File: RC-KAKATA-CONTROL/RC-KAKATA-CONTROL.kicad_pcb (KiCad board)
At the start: 4 copper layers, 160 x 160 mm, 178 parts, among them J1 Conn_02x20_Socket_DG250T-5.0-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, J10 DB125-2.54-4P-GN, J11 Screw_Terminal_01x02, J12 Conn_01x07, J13 Screw_Terminal_01x02, J15 Conn_01x12_Socket, J17 Screw_Terminal_01x02, J19 Screw_Terminal_01x02, J2 Screw_Terminal_01x02, J21 Screw_Terminal_01x02, J23 Screw_Terminal_01x02, J25 Conn_02x20_Socket_DG250T-5.0-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, J3 Screw_Terminal_01x02, J4 Screw_Terminal_01x02, J5 Screw_Terminal_01x02, J6 Raspberry_Pi_2x20_PTH, J7 Screw_Terminal_01x02, J8 DB125-2.54-4P-GN, J9 Screw_Terminal_01x02, SW1 TS-1088-AR02016, SW2 TS-1088-AR02016, SW3 TS-1088-AR02016, SW4 TS-1088-AR02016, SW6 TS-1088-AR02016, U1 PS-TO220, U13 ICM-20689, U2 PS-TO220, U3 STM32H743IIT6, U4 YK16S-L7.2-B10KA(32-8)-G-A29, U5 DB125-2.54-6P-GN, U8 W25Q128JVSIQTR, X1 SMD3225-4, X2 Q13MC3061000300

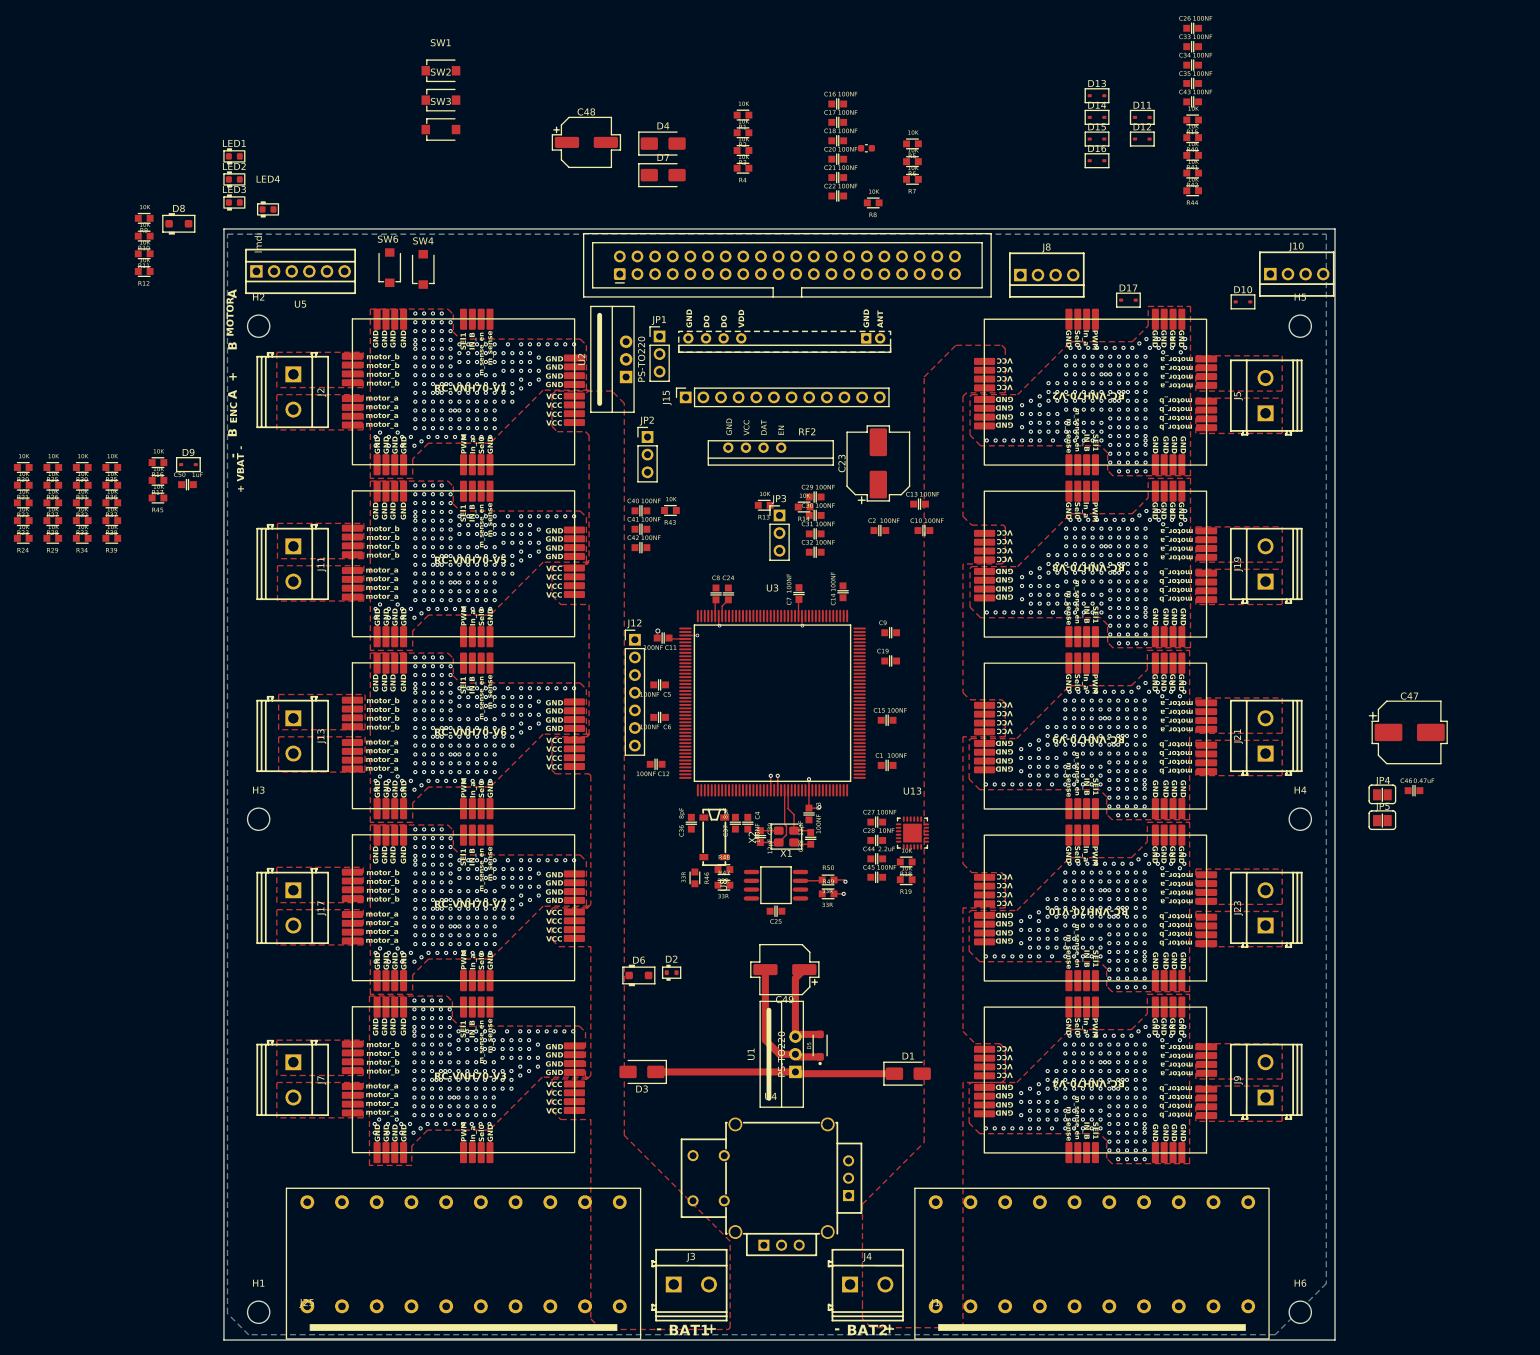
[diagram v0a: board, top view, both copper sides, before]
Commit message: Agregadas conexiones de analogicos Agregadas las conexiones de i2c Agregadas las conexiones de Uart Cambiados algunos detalles de tvs resistencias y cap Recolocados los componenetes de power supply Cambiados los diodos de entrada de la bateria por unos de 5A Cambios menores y mejorada la documentacion Agregada informacion en la serigrafia del PCB
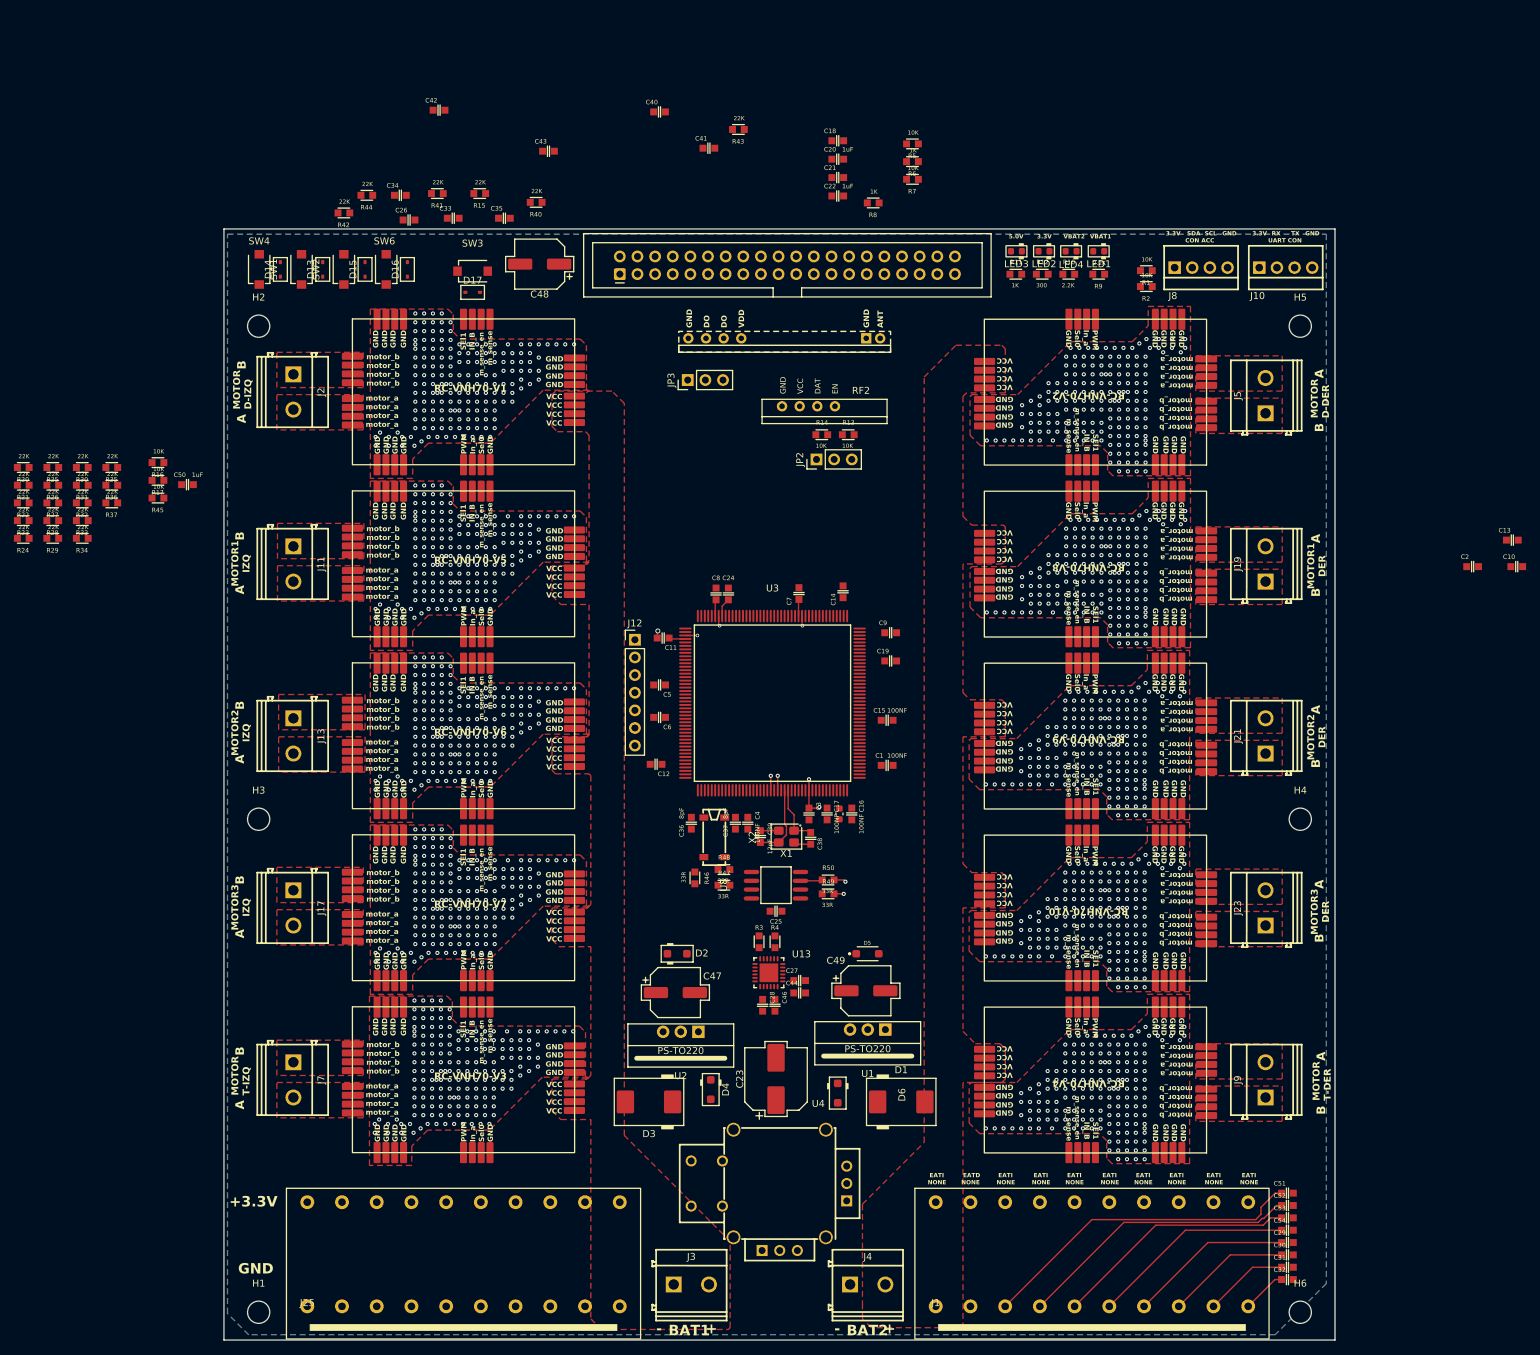
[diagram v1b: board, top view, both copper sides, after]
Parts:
- removed C45: 100NF, 4ms_Capacitor:C_0603
- removed D10, D11, D12, D9: PESD3V3L1BA, Diode_SMD_AKL:D_SOD-323_TVS
- removed D7: SS26, Diode_SMD:D_SMA
- removed D8: SMF24CA, Diode_SMD_AKL:D_SOD-123F
- removed J15: Conn_01x12_Socket, Connector_PinSocket_2.54mm:PinSocket_1x12_P2.54mm_Vertical
- removed JP1: Jumper_3_Bridged12, Connector_PinHeader_2.54mm:PinHeader_1x03_P2.54mm_Vertical
- removed JP4, JP5: SolderJumper_2_Open, 4ms_SolderJumper:JUMPER_SMD_1x2
- removed R18, R19, R38, R39: 10K, 4ms_Resistor:R_0603
- removed U5: DB125-2.54-6P-GN, EasyEDA:CONN-TH_DB125-2.54-6P-GN
- added C51: 100NF, 4ms_Capacitor:C_0603, F.Cu at (247.7, 196.8)
- added C52: 100NF, 4ms_Capacitor:C_0603, F.Cu at (247.7, 198.6)
- added C53: 100NF, 4ms_Capacitor:C_0603, F.Cu at (247.7, 200.4)
- added C54: 100NF, 4ms_Capacitor:C_0603, F.Cu at (247.7, 202.2)
- C20, C22: value 100NF -> 1uF
- C23: value CP_SMD_D8.0mm_H6.2mm -> 100uF
- C47: footprint Capacitor_SMD_AKL:CP_Elec_8x6.2 -> Capacitor_SMD_AKL:CP_Elec_6.3x5.9
- C48, C49: value CP_SMD_D6.3mm_H5.9mm -> 100uF
- D1, D3: value SS26 -> SS54; footprint Diode_SMD:D_SMA -> Diode_SMD_AKL:D_SMC
- D2: value ESD5B5.0S -> SMF5.0A; footprint Diode_SMD_AKL:D_SOD-523 -> Diode_SMD_AKL:D_SOD-123F
- D4: value SS26 -> SMF24CA; footprint Diode_SMD:D_SMA -> Diode_SMD_AKL:D_SOD-123F
- R10, R9: value 10K -> 2.2K
- R11, R6, R8: value 10K -> 1K
- R12: value 10K -> 300
- R15, R20, R21, R22, R23, R24, R25, R26, R27, R28, R29, R30, R31, R32, R33, R34, R35, R36, R37, R40, R41, R42, R43, R44: value 10K -> 22K
- moved R9 137.7 mm to (220.5, 64.5)
- moved D4 136.4 mm to (164.6, 181.9), turned to -90 degrees
- moved R10 133.3 mm to (216.2, 64.5), turned to 180 degrees
- moved R12 129.3 mm to (212.3, 64.5), turned to 180 degrees
- moved C29 127.1 mm to (247.7, 204.0)
- moved C30 126.4 mm to (247.7, 205.7)
- moved C31 125.6 mm to (247.7, 207.5)
- moved R11 125.6 mm to (208.5, 64.5), turned to 180 degrees
- moved LED1 125.2 mm to (220.5, 61.2), turned to 180 degrees
- moved C32 124.9 mm to (247.7, 209.3)
- moved R42 122.4 mm to (111.8, 55.7)
- moved D14 119.6 mm to (102.6, 63.8), turned to 90 degrees
- moved R44 118.9 mm to (115.1, 53.2)
- moved LED2 117.1 mm to (212.6, 61.2), turned to 180 degrees
- moved C26 116.2 mm to (121.2, 56.7)
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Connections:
- C23 pad 1: /power_supply/VDC_IN_VDD3 -> Net-(D1-K)
- C26 pad 1: /nrst -> /NJTRST
- C29 pad 1: /LSGTD -> /LS_DELANTERO_DX_180G
- C30 pad 1: /LSGTI -> /LS_DELANTERO_DX_0G
- C31 pad 1: /LS_GDD -> /LS_DELANTERO_IX_180G
- C32 pad 1: /LS_GDI -> /LS_DELANTERO_IX_0G
- C47 pad 1: /power_supply/VDC_IN_VDD5 -> +5V
- D1 pad 1: /power_supply/VDC_IN_VDD3 -> Net-(D1-K)
- D17 pad 2: /nrst -> /NJTRST
- D3 pad 1: /power_supply/VDC_IN_VDD3 -> Net-(D1-K)
- D4 pad 1: /power_supply/VDC_IN_VDD5 -> GND
- D4 pad 2: /VBAT_1 -> Net-(D1-K)
- D5 pad A: +3.3V -> GND
- D5 pad C: GND -> +3.3V
- D6 pad 2: /power_supply/VDC_IN_VDD3 -> Net-(D1-K)
- J1 pad 1: /ENC_B_MOTOR_3_DER -> unconnected-(J1-Pin_1-Pad1)
- J1 pad 10: /ENC_B_TRASERO_IZQ -> /LS_DELANTERO_IX_0G
- J1 pad 2: /ENC_B_MOTOR_2_DER -> unconnected-(J1-Pin_2-Pad2)
- J1 pad 3: /ENC_B_MOTOR_1_DER -> /LS_TRASERO_DX_180G
- J1 pad 4: /ENC_B_MOTOR_3_IZQ -> /LS_TRASERO_DX_0G
- J1 pad 5: /ENC_B_MOTOR_2_IZQ -> /LS_TRASERO_IX_180G
- J1 pad 6: /ENC_B_MOTOR_1_IZQ -> /LS_TRASERO_IX_0G
- J1 pad 7: /ENC_B_DELANTERO_DER -> /LS_DELANTERO_DX_180G
- J1 pad 8: /ENC_B_DELANTERO_IZQ -> /LS_DELANTERO_DX_0G
- J1 pad 9: /ENC_B_TRASERO_DER -> /LS_DELANTERO_IX_180G
- JP3 pad 2: Net-(JP1-C) -> Net-(JP3-C)
- R1 pad 2: /LS_GDI -> /ACC_I2C_SCL
- R15 pad 2: /nrst -> /NJTRST
- R2 pad 2: /LS_GDD -> /ACC_I2C_SDA
- R3 pad 2: /LSGTI -> /ACC_GYR_SDA
- R30 pad 2: /ENC_B_TRASERO_IZQ -> /LS_DELANTERO_IX_0G
- R31 pad 2: /ENC_B_TRASERO_DER -> /LS_DELANTERO_IX_180G
- R32 pad 2: /ENC_B_DELANTERO_IZQ -> /LS_DELANTERO_DX_0G
- R33 pad 2: /ENC_B_DELANTERO_DER -> /LS_DELANTERO_DX_180G
- R34 pad 2: /ENC_B_MOTOR_1_IZQ -> /LS_TRASERO_IX_0G
- R35 pad 2: /ENC_B_MOTOR_2_IZQ -> /LS_TRASERO_IX_180G
- R36 pad 2: /ENC_B_MOTOR_3_IZQ -> /LS_TRASERO_DX_0G
- R37 pad 2: /ENC_B_MOTOR_1_DER -> /LS_TRASERO_DX_180G
- R4 pad 2: /LSGTD -> /ACC_GYR_SCL
- RF1 pad 2: unconnected-(RF1-GND-Pad2) -> GND
- RF1 pad 4: Net-(JP1-A) -> Net-(JP3-C)
- RF1 pad 5: Net-(JP1-A) -> Net-(JP3-C)
- SW3 pad 2: /nrst -> /NJTRST
- U1 pad 1: /power_supply/VDC_IN_VDD3 -> Net-(D1-K)
- U13 pad 9: /acc-gyr/AD0/SDO -> GND
- U2 pad 1: /power_supply/VDC_IN_VDD5 -> Net-(D1-K)
- U3 pad 106: unconnected-(U3-PG2-Pad106) -> /DIR_A_TRASERO_DER
- U3 pad 107: unconnected-(U3-PG3-Pad107) -> /DIR_B_TRASERO_DER
- U3 pad 108: unconnected-(U3-PG4-Pad108) -> /DIR_A_DELANTERO_IZQ
- U3 pad 109: unconnected-(U3-PG5-Pad109) -> /DIR_B_DELANTERO_IZQ
- U3 pad 11: unconnected-(U3-PI9-Pad11) -> /LS_TRASERO_IX_180G
- U3 pad 110: unconnected-(U3-PG6-Pad110) -> /DIR_A_DELANTERO_DER
- U3 pad 111: unconnected-(U3-PG7-Pad111) -> /DIR_B_DELANTERO_DER
- U3 pad 112: unconnected-(U3-PG8-Pad112) -> /DIR_A_MOTOR_IZQ
- U3 pad 12: unconnected-(U3-PI10-Pad12) -> /LS_TRASERO_DX_0G
- U3 pad 13: unconnected-(U3-PI11-Pad13) -> /LS_TRASERO_DX_180G
- U3 pad 131: unconnected-(U3-PI0-Pad131) -> /BUTON1
- U3 pad 132: unconnected-(U3-PI1-Pad132) -> /BUTON2
- U3 pad 133: unconnected-(U3-PI2-Pad133) -> /BUTON3
- U3 pad 134: unconnected-(U3-PI3-Pad134) -> /BUTON4
- U3 pad 152: unconnected-(U3-PG9-Pad152) -> /DIR_B_MOTOR_IZQ
- U3 pad 153: unconnected-(U3-PG10-Pad153) -> /DIR_A_MOTOR_DER
- U3 pad 154: unconnected-(U3-PG11-Pad154) -> /DIR_B_MOTOR_DER
- U3 pad 155: unconnected-(U3-PG12-Pad155) -> /JOY_PB
- U3 pad 156: unconnected-(U3-PG13-Pad156) -> /ACC_GYR_INT
- U3 pad 16: unconnected-(U3-PF0-Pad16) -> /ACC_GYR_SDA
- U3 pad 164: unconnected-(U3-PB6-Pad164) -> /ACC_I2C_SCL
- U3 pad 165: unconnected-(U3-PB7-Pad165) -> /ACC_I2C_SDA
- U3 pad 17: unconnected-(U3-PF1-Pad17) -> /ACC_GYR_SCL
- U3 pad 173: unconnected-(U3-PI4-Pad173) -> /LS_DELANTERO_IX_0G
- U3 pad 174: unconnected-(U3-PI5-Pad174) -> /LS_DELANTERO_IX_180G
- U3 pad 175: unconnected-(U3-PI6-Pad175) -> /LS_DELANTERO_DX_0G
- U3 pad 176: unconnected-(U3-PI7-Pad176) -> /LS_DELANTERO_DX_180G
- U3 pad 56: unconnected-(U3-PB0-Pad56) -> /JOY_DIRA
- U3 pad 57: unconnected-(U3-PB1-Pad57) -> /JOY_DIRB
- U3 pad 66: unconnected-(U3-PG0-Pad66) -> /DIR_A_TRASERO_IZQ
- U3 pad 67: unconnected-(U3-PG1-Pad67) -> /DIR_B_TRASERO_IZQ
- U3 pad 7: unconnected-(U3-PI8-Pad7) -> /LS_TRASERO_IX_0G
- U3 pad 92: unconnected-(U3-PB12-Pad92) -> /UART_RX
- U3 pad 93: unconnected-(U3-PB13-Pad93) -> /UART_TX
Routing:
- net /LS_TRASERO_DX_180G: track 0.00 -> 47.1 mm
- net /LS_TRASERO_DX_0G: track 0.00 -> 40.8 mm
- net /LS_TRASERO_IX_180G: track 0.00 -> 35.1 mm
- net /power_supply/VDC_IN_VDD3: track 34.5 -> 0.00 mm
- net /LS_TRASERO_IX_0G: track 0.00 -> 29.3 mm
- net /LS_DELANTERO_DX_180G: track 0.00 -> 23.6 mm
- net GND: track 30.0 -> 11.0 mm
- net /LS_DELANTERO_DX_0G: track 0.00 -> 17.9 mm
- net +3.3V: track 26.8 -> 12.9 mm
- net /LS_DELANTERO_IX_180G: track 0.00 -> 12.1 mm
- net /LS_DELANTERO_IX_0G: track 0.00 -> 6.40 mm
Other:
- board text added: "+3.3V"
- board text added: "3.3V"
- board text added: "5.0V"
- board text added: "CON ACC"
- board text added: "EATD"
- board text added: "EATI"
- board text added: "GND"
- board text added: "MOTOR D-DER"
- board text added: "MOTOR D-IZQ"
- board text added: "MOTOR T-DER"
- board text added: "MOTOR T-IZQ"
- board text added: "MOTOR1 DER"
- board text added: "MOTOR1 IZQ"
- board text added: "MOTOR2 DER"
- board text added: "MOTOR2 IZQ"
- board text added: "MOTOR3 DER"
- board text added: "MOTOR3 IZQ"
- board text added: "NONE"
- board text added: "RX"
- board text added: "SCL"
- board text added: "SDA"
- board text added: "TX"
- board text added: "UART CON"
- board text added: "VBAT1"
- board text added: "VBAT2"
- board text removed: "+ VBAT -"
- board text removed: "ENC"
- board text removed: "MOTOR"
- board text removed: "lmdi"
